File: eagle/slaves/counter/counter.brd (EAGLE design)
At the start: 126.2 x 32 mm, 92 parts, among them IC1 MCP1703DB, IC2 4067D, IC3 74HC154DW, J1 RJ12RIGHTANGLE-I2C, X2 8MHz, X4 MINI-USB

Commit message: change resistor for led
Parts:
- RK11, RK13, RK17, RK19, RK21, RK23, RK25, RK27, RK29, RK31, RK33, RK35, RK41, RK43, RK5, RK9: value 1k -> 100
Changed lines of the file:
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@@
 <?xml version="1.0" encoding="utf-8"?>
 <!DOCTYPE eagle SYSTEM "eagle.dtd">
-<eagle version="8.3.0">
+<eagle version="9.0.0">
 <drawing>
 <settings>
-<setting alwaysvectorfont="yes"/>
+<setting alwaysvectorfont="no"/>
 <setting keepoldvectorfont="yes"/>
 <setting verticaltext="up"/>
@@
 <param name="dpMaxLengthDifference" value="10mm"/>
 <param name="dpGapFactor" value="2.5"/>
-<param name="checkGrid" value="0"/>
 <param name="checkAngle" value="0"/>
 <param name="checkFont" value="1"/>
 <param name="checkRestrict" value="0"/>
+<param name="checkStop" value="0"/>
+<param name="checkValues" value="0"/>
 <param name="useDiameter" value="13"/>
 <param name="maxErrors" value="50"/>
@@
 <element name="IC3" library="74xx-eu" library_urn="urn:adsk.eagle:library:85" package="SO24W" value="74HC154DW" x="50.92" y="24.3625" rot="R270"/>
 <element name="O3" library="SparkFun" package="QRE1113" value="QRE1113" x="3.81" y="12.7" smashed="yes" rot="MR180"/>
-<element name="RK5" library="resistor" package="M0805" value="1k" x="2.54" y="12.7" smashed="yes" rot="R90">
+<element name="RK5" library="resistor" package="M0805" value="100" x="2.54" y="12.7" smashed="yes" rot="R90">
 <attribute name="NAME" x="1.27" y="11.43" size="1.27" layer="25" rot="R90"/>
 <attribute name="VALUE" x="1.42875" y="11.7475" size="1.27" layer="27" rot="R90"/>
@@
 </element>
 <element name="O4" library="SparkFun" package="QRE1113" value="QRE1113" x="3.81" y="3.81" smashed="yes" rot="MR0"/>
-<element name="RK9" library="resistor" package="M0805" value="1k" x="5.08" y="3.81" smashed="yes" rot="R270">
+<element name="RK9" library="resistor" package="M0805" value="100" x="5.08" y="3.81" smashed="yes" rot="R270">
 <attribute name="NAME" x="6.35" y="5.08" size="1.27" layer="25" rot="R270"/>
 <attribute name="VALUE" x="6.0325" y="4.1275" size="1.27" layer="27" rot="R270"/>
@@
 </element>
 <element name="O5" library="SparkFun" package="QRE1113" value="QRE1113" x="16.51" y="12.7" smashed="yes" rot="MR180"/>
-<element name="RK11" library="resistor" package="M0805" value="1k" x="15.24" y="12.7" smashed="yes" rot="R90">
+<element name="RK11" library="resistor" package="M0805" value="100" x="15.24" y="12.7" smashed="yes" rot="R90">
 <attribute name="NAME" x="13.97" y="11.43" size="1.27" layer="25" rot="R90"/>
 <attribute name="VALUE" x="14.12875" y="11.7475" size="1.27" layer="27" rot="R90"/>
@@
 </element>
 <element name="O6" library="SparkFun" package="QRE1113" value="QRE1113" x="16.51" y="3.81" smashed="yes" rot="MR0"/>
-<element name="RK13" library="resistor" package="M0805" value="1k" x="17.78" y="3.81" smashed="yes" rot="R270">
+<element name="RK13" library="resistor" package="M0805" value="100" x="17.78" y="3.81" smashed="yes" rot="R270">
 <attribute name="NAME" x="19.05" y="5.08" size="1.27" layer="25" rot="R270"/>
 <attribute name="VALUE" x="18.7325" y="4.1275" size="1.27" layer="27" rot="R270"/>
@@
 </element>
 <element name="O9" library="SparkFun" package="QRE1113" value="QRE1113" x="29.21" y="12.7" smashed="yes" rot="MR180"/>
-<element name="RK21" library="resistor" package="M0805" value="1k" x="27.94" y="12.7" smashed="yes" rot="R90">
+<element name="RK21" library="resistor" package="M0805" value="100" x="27.94" y="12.7" smashed="yes" rot="R90">
 <attribute name="NAME" x="26.67" y="11.43" size="1.27" layer="25" rot="R90"/>
 <attribute name="VALUE" x="26.82875" y="11.7475" size="1.27" layer="27" rot="R90"/>
@@
 </element>
 <element name="O10" library="SparkFun" package="QRE1113" value="QRE1113" x="29.21" y="3.81" smashed="yes" rot="MR0"/>
-<element name="RK23" library="resistor" package="M0805" value="1k" x="30.48" y="3.81" smashed="yes" rot="R270">
+<element name="RK23" library="resistor" package="M0805" value="100" x="30.48" y="3.81" smashed="yes" rot="R270">
 <attribute name="NAME" x="31.75" y="5.08" size="1.27" layer="25" rot="R270"/>
 <attribute name="VALUE" x="31.4325" y="4.1275" size="1.27" layer="27" rot="R270"/>
@@
 </element>
 <element name="O13" library="SparkFun" package="QRE1113" value="QRE1113" x="42.545" y="12.7" smashed="yes" rot="MR180"/>
-<element name="RK29" library="resistor" package="M0805" value="1k" x="41.275" y="12.7" smashed="yes" rot="R90">
+<element name="RK29" library="resistor" package="M0805" value="100" x="41.275" y="12.7" smashed="yes" rot="R90">
 <attribute name="NAME" x="40.005" y="11.43" size="1.27" layer="25" rot="R90"/>
 <attribute name="VALUE" x="40.16375" y="11.7475" size="1.27" layer="27" rot="R90"/>
@@
 </element>
 <element name="O14" library="SparkFun" package="QRE1113" value="QRE1113" x="42.545" y="3.81" smashed="yes" rot="MR0"/>
-<element name="RK31" library="resistor" package="M0805" value="1k" x="43.815" y="3.81" smashed="yes" rot="R270">
+<element name="RK31" library="resistor" package="M0805" value="100" x="43.815" y="3.81" smashed="yes" rot="R270">
 <attribute name="NAME" x="45.085" y="5.08" size="1.27" layer="25" rot="R270"/>
 <attribute name="VALUE" x="44.7675" y="4.1275" size="1.27" layer="27" rot="R270"/>
@@
 </element>
 <element name="O7" library="SparkFun" package="QRE1113" value="QRE1113" x="55.88" y="12.7" smashed="yes" rot="MR180"/>
-<element name="RK17" library="resistor" package="M0805" value="1k" x="54.61" y="12.7" smashed="yes" rot="R90">
+<element name="RK17" library="resistor" package="M0805" value="100" x="54.61" y="12.7" smashed="yes" rot="R90">
 <attribute name="NAME" x="53.34" y="11.43" size="1.27" layer="25" rot="R90"/>
 <attribute name="VALUE" x="53.49875" y="11.7475" size="1.27" layer="27" rot="R90"/>
@@
 </element>
 <element name="O8" library="SparkFun" package="QRE1113" value="QRE1113" x="55.88" y="3.81" smashed="yes" rot="MR0"/>
-<element name="RK19" library="resistor" package="M0805" value="1k" x="57.15" y="3.81" smashed="yes" rot="R270">
+<element name="RK19" library="resistor" package="M0805" value="100" x="57.15" y="3.81" smashed="yes" rot="R270">
 <attribute name="NAME" x="58.42" y="5.08" size="1.27" layer="25" rot="R270"/>
 <attribute name="VALUE" x="58.1025" y="4.1275" size="1.27" layer="27" rot="R270"/>
@@
 </element>
 <element name="O15" library="SparkFun" package="QRE1113" value="QRE1113" x="69.215" y="12.7" smashed="yes" rot="MR180"/>
-<element name="RK33" library="resistor" package="M0805" value="1k" x="67.945" y="12.7" smashed="yes" rot="R90">
+<element name="RK33" library="resistor" package="M0805" value="100" x="67.945" y="12.7" smashed="yes" rot="R90">
 <attribute name="NAME" x="66.675" y="11.43" size="1.27" layer="25" rot="R90"/>
 <attribute name="VALUE" x="66.83375" y="11.7475" size="1.27" layer="27" rot="R90"/>
@@
 </element>
 <element name="O16" library="SparkFun" package="QRE1113" value="QRE1113" x="69.215" y="3.81" smashed="yes" rot="MR0"/>
-<element name="RK35" library="resistor" package="M0805" value="1k" x="70.485" y="3.81" smashed="yes" rot="R270">
+<element name="RK35" library="resistor" package="M0805" value="100" x="70.485" y="3.81" smashed="yes" rot="R270">
 <attribute name="NAME" x="71.755" y="5.08" size="1.27" layer="25" rot="R270"/>
 <attribute name="VALUE" x="71.4375" y="4.1275" size="1.27" layer="27" rot="R270"/>
@@
 </element>
 <element name="O19" library="SparkFun" package="QRE1113" value="QRE1113" x="82.55" y="12.7" smashed="yes" rot="MR180"/>
-<element name="RK41" library="resistor" package="M0805" value="1k" x="81.28" y="12.7" smashed="yes" rot="R90">
+<element name="RK41" library="resistor" package="M0805" value="100" x="81.28" y="12.7" smashed="yes" rot="R90">
 <attribute name="NAME" x="80.01" y="11.43" size="1.27" layer="25" rot="R90"/>
 <attribute name="VALUE" x="80.16875" y="11.7475" size="1.27" layer="27" rot="R90"/>
@@
 </element>
 <element name="O20" library="SparkFun" package="QRE1113" value="QRE1113" x="82.55" y="3.81" smashed="yes" rot="MR0"/>
-<element name="RK43" library="resistor" package="M0805" value="1k" x="83.82" y="3.81" smashed="yes" rot="R270">
+<element name="RK43" library="resistor" package="M0805" value="100" x="83.82" y="3.81" smashed="yes" rot="R270">
 <attribute name="NAME" x="85.09" y="5.08" size="1.27" layer="25" rot="R270"/>
 <attribute name="VALUE" x="84.7725" y="4.1275" size="1.27" layer="27" rot="R270"/>
@@
 </element>
 <element name="O11" library="SparkFun" package="QRE1113" value="QRE1113" x="95.25" y="12.7" smashed="yes" rot="MR180"/>
-<element name="RK25" library="resistor" package="M0805" value="1k" x="93.98" y="12.7" smashed="yes" rot="R90">
+<element name="RK25" library="resistor" package="M0805" value="100" x="93.98" y="12.7" smashed="yes" rot="R90">
 <attribute name="NAME" x="92.71" y="11.43" size="1.27" layer="25" rot="R90"/>
 <attribute name="VALUE" x="92.86875" y="11.7475" size="1.27" layer="27" rot="R90"/>
@@
 </element>
 <element name="O12" library="SparkFun" package="QRE1113" value="QRE1113" x="95.25" y="3.81" smashed="yes" rot="MR0"/>
-<element name="RK27" library="resistor" package="M0805" value="1k" x="96.52" y="3.81" smashed="yes" rot="R270">
+<element name="RK27" library="resistor" package="M0805" value="100" x="96.52" y="3.81" smashed="yes" rot="R270">
 <attribute name="NAME" x="97.79" y="5.08" size="1.27" layer="25" rot="R270"/>
 <attribute name="VALUE" x="97.4725" y="4.1275" size="1.27" layer="27" rot="R270"/>
@@
 </signal>
 </signals>
-<errors>
-</errors>
 </board>
 </drawing>

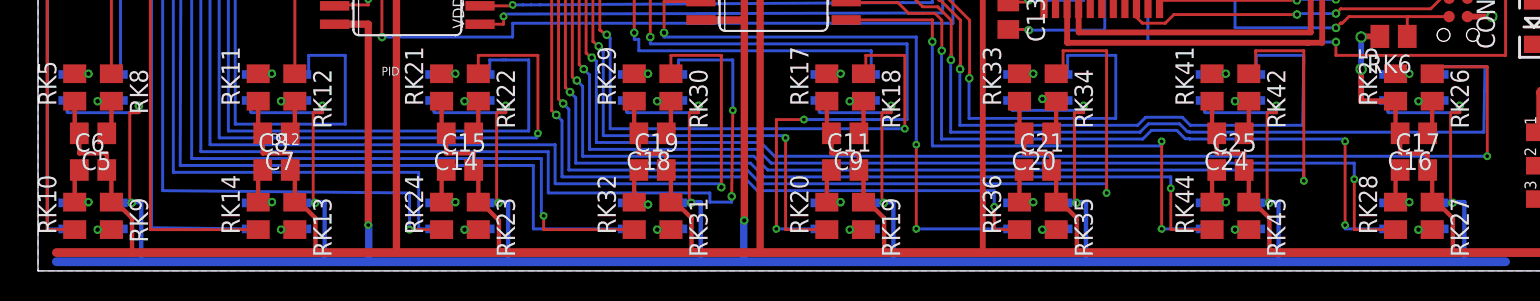
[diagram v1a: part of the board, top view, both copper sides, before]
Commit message: remove 10nf capacitor
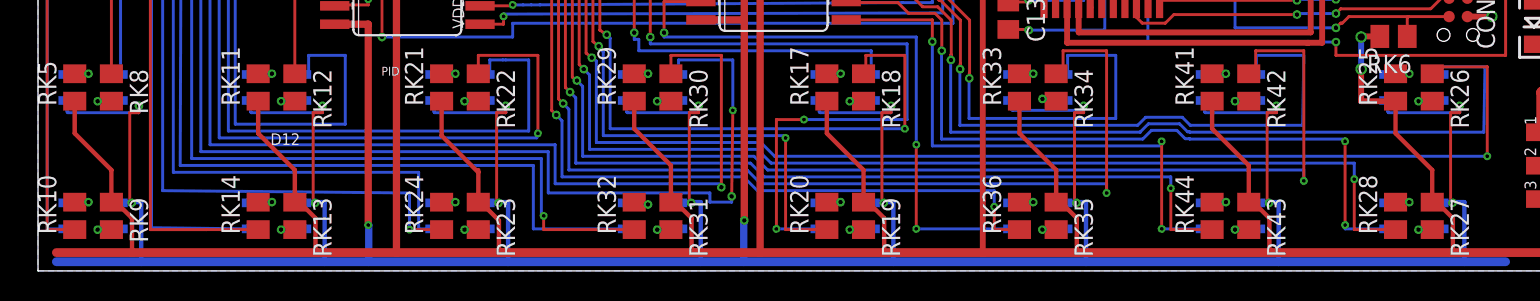
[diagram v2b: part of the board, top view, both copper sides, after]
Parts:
- removed C11, C14, C15, C16, C17, C18, C19, C20, C21, C24, C25, C5, C6, C7, C8, C9: 10n, rcl:C0805
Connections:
- net 3.3V: no longer C11.2, C14.2, C15.2, C16.2, C17.2, C18.2, C19.2, C20.2, C21.2, C24.2, C25.2, C5.2, C6.2, C7.2, C8.2, C9.2
- net Y10: no longer C15.1
- net Y11: no longer C16.1
- net Y12: no longer C17.1
- net Y13: no longer C18.1
- net Y14: no longer C19.1
- net Y15: no longer C20.1
- net Y16: no longer C21.1
- net Y19: no longer C24.1
- net Y20: no longer C25.1
- net Y3: no longer C5.1
- net Y4: no longer C6.1
- net Y5: no longer C7.1
- net Y6: no longer C8.1
- net Y7: no longer C9.1
- net Y8: no longer C11.1
- net Y9: no longer C14.1
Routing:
- net 3.3V: track 379.2 -> 369.0 mm
- net Y16: track 5.03 -> 2.49 mm
- net Y8: track 5.04 -> 2.49 mm
- net Y6: track 5.03 -> 2.49 mm
- net Y14: track 5.10 -> 2.56 mm
- net Y10: track 5.03 -> 2.49 mm
- net Y4: track 5.04 -> 2.49 mm
- net Y20: track 5.03 -> 2.49 mm
- net Y12: track 5.03 -> 2.49 mm
- net Y3: track 4.85 -> 2.49 mm
- net Y9: track 4.85 -> 2.49 mm
- net Y7: track 4.85 -> 2.49 mm
- net Y5: track 4.85 -> 2.49 mm
- net Y13: track 4.85 -> 2.49 mm
- net Y19: track 4.85 -> 2.49 mm
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
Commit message: change resistor to 1k
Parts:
- RK10, RK12, RK14, RK18, RK20, RK22, RK24, RK26, RK28, RK30, RK32, RK34, RK36, RK42, RK44, RK8: value 220 -> 1k
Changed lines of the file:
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@@
 <grid distance="6.25" unitdist="mil" unit="mil" style="lines" multiple="10" display="yes" altdistance="3.125" altunitdist="mil" altunit="mil"/>
 <layers>
-<layer number="1" name="Top" color="4" fill="1" visible="yes" active="yes"/>
+<layer number="1" name="Top" color="4" fill="1" visible="no" active="yes"/>
 <layer number="16" name="Bottom" color="1" fill="1" visible="yes" active="yes"/>
 <layer number="17" name="Pads" color="2" fill="1" visible="yes" active="yes"/>
@@
 <attribute name="VALUE" x="1.42875" y="11.7475" size="1.27" layer="27" rot="R90"/>
 </element>
-<element name="RK8" library="resistor" package="M0805" value="220" x="5.08" y="12.7" smashed="yes" rot="R270">
+<element name="RK8" library="resistor" package="M0805" value="1k" x="5.08" y="12.7" smashed="yes" rot="R270">
 <attribute name="NAME" x="6.35" y="13.97" size="1.27" layer="25" rot="R270"/>
 <attribute name="VALUE" x="6.19125" y="14.605" size="1.27" layer="27" rot="R270"/>
@@
 <attribute name="VALUE" x="6.0325" y="4.1275" size="1.27" layer="27" rot="R270"/>
 </element>
-<element name="RK10" library="resistor" package="M0805" value="220" x="2.54" y="3.81" smashed="yes" rot="R90">
+<element name="RK10" library="resistor" package="M0805" value="1k" x="2.54" y="3.81" smashed="yes" rot="R90">
 <attribute name="NAME" x="1.27" y="2.54" size="1.27" layer="25" rot="R90"/>
 <attribute name="VALUE" x="1.42875" y="2.54" size="1.27" layer="27" rot="R90"/>
@@
 <attribute name="VALUE" x="14.12875" y="11.7475" size="1.27" layer="27" rot="R90"/>
 </element>
-<element name="RK12" library="resistor" package="M0805" value="220" x="17.78" y="12.7" smashed="yes" rot="R270">
+<element name="RK12" library="resistor" package="M0805" value="1k" x="17.78" y="12.7" smashed="yes" rot="R270">
 <attribute name="NAME" x="19.05" y="13.97" size="1.27" layer="25" rot="R270"/>
 <attribute name="VALUE" x="18.89125" y="14.605" size="1.27" layer="27" rot="R270"/>
@@
 <attribute name="VALUE" x="18.7325" y="4.1275" size="1.27" layer="27" rot="R270"/>
 </element>
-<element name="RK14" library="resistor" package="M0805" value="220" x="15.24" y="3.81" smashed="yes" rot="R90">
+<element name="RK14" library="resistor" package="M0805" value="1k" x="15.24" y="3.81" smashed="yes" rot="R90">
 <attribute name="NAME" x="13.97" y="2.54" size="1.27" layer="25" rot="R90"/>
 <attribute name="VALUE" x="14.12875" y="2.54" size="1.27" layer="27" rot="R90"/>
@@
 <attribute name="VALUE" x="26.82875" y="11.7475" size="1.27" layer="27" rot="R90"/>
 </element>
-<element name="RK22" library="resistor" package="M0805" value="220" x="30.48" y="12.7" smashed="yes" rot="R270">
+<element name="RK22" library="resistor" package="M0805" value="1k" x="30.48" y="12.7" smashed="yes" rot="R270">
 <attribute name="NAME" x="31.75" y="13.97" size="1.27" layer="25" rot="R270"/>
 <attribute name="VALUE" x="31.59125" y="14.605" size="1.27" layer="27" rot="R270"/>
@@
 <attribute name="VALUE" x="31.4325" y="4.1275" size="1.27" layer="27" rot="R270"/>
 </element>
-<element name="RK24" library="resistor" package="M0805" value="220" x="27.94" y="3.81" smashed="yes" rot="R90">
+<element name="RK24" library="resistor" package="M0805" value="1k" x="27.94" y="3.81" smashed="yes" rot="R90">
 <attribute name="NAME" x="26.67" y="2.54" size="1.27" layer="25" rot="R90"/>
 <attribute name="VALUE" x="26.82875" y="2.54" size="1.27" layer="27" rot="R90"/>
@@
 <attribute name="VALUE" x="40.16375" y="11.7475" size="1.27" layer="27" rot="R90"/>
 </element>
-<element name="RK30" library="resistor" package="M0805" value="220" x="43.815" y="12.7" smashed="yes" rot="R270">
+<element name="RK30" library="resistor" package="M0805" value="1k" x="43.815" y="12.7" smashed="yes" rot="R270">
 <attribute name="NAME" x="45.085" y="13.97" size="1.27" layer="25" rot="R270"/>
 <attribute name="VALUE" x="44.92625" y="14.605" size="1.27" layer="27" rot="R270"/>
@@
 <attribute name="VALUE" x="44.7675" y="4.1275" size="1.27" layer="27" rot="R270"/>
 </element>
-<element name="RK32" library="resistor" package="M0805" value="220" x="41.275" y="3.81" smashed="yes" rot="R90">
+<element name="RK32" library="resistor" package="M0805" value="1k" x="41.275" y="3.81" smashed="yes" rot="R90">
 <attribute name="NAME" x="40.005" y="2.54" size="1.27" layer="25" rot="R90"/>
 <attribute name="VALUE" x="40.16375" y="2.54" size="1.27" layer="27" rot="R90"/>
@@
 <attribute name="VALUE" x="53.49875" y="11.7475" size="1.27" layer="27" rot="R90"/>
 </element>
-<element name="RK18" library="resistor" package="M0805" value="220" x="57.15" y="12.7" smashed="yes" rot="R270">
+<element name="RK18" library="resistor" package="M0805" value="1k" x="57.15" y="12.7" smashed="yes" rot="R270">
 <attribute name="NAME" x="58.42" y="13.97" size="1.27" layer="25" rot="R270"/>
 <attribute name="VALUE" x="58.26125" y="14.605" size="1.27" layer="27" rot="R270"/>
@@
 <attribute name="VALUE" x="58.1025" y="4.1275" size="1.27" layer="27" rot="R270"/>
 </element>
-<element name="RK20" library="resistor" package="M0805" value="220" x="54.61" y="3.81" smashed="yes" rot="R90">
+<element name="RK20" library="resistor" package="M0805" value="1k" x="54.61" y="3.81" smashed="yes" rot="R90">
 <attribute name="NAME" x="53.34" y="2.54" size="1.27" layer="25" rot="R90"/>
 <attribute name="VALUE" x="53.49875" y="2.54" size="1.27" layer="27" rot="R90"/>
@@
 <attribute name="VALUE" x="66.83375" y="11.7475" size="1.27" layer="27" rot="R90"/>
 </element>
-<element name="RK34" library="resistor" package="M0805" value="220" x="70.485" y="12.7" smashed="yes" rot="R270">
+<element name="RK34" library="resistor" package="M0805" value="1k" x="70.485" y="12.7" smashed="yes" rot="R270">
 <attribute name="NAME" x="71.755" y="13.97" size="1.27" layer="25" rot="R270"/>
 <attribute name="VALUE" x="71.59625" y="14.605" size="1.27" layer="27" rot="R270"/>
@@
 <attribute name="VALUE" x="71.4375" y="4.1275" size="1.27" layer="27" rot="R270"/>
 </element>
-<element name="RK36" library="resistor" package="M0805" value="220" x="67.945" y="3.81" smashed="yes" rot="R90">
+<element name="RK36" library="resistor" package="M0805" value="1k" x="67.945" y="3.81" smashed="yes" rot="R90">
 <attribute name="NAME" x="66.675" y="2.54" size="1.27" layer="25" rot="R90"/>
 <attribute name="VALUE" x="66.83375" y="2.54" size="1.27" layer="27" rot="R90"/>
@@
 <attribute name="VALUE" x="80.16875" y="11.7475" size="1.27" layer="27" rot="R90"/>
 </element>
-<element name="RK42" library="resistor" package="M0805" value="220" x="83.82" y="12.7" smashed="yes" rot="R270">
+<element name="RK42" library="resistor" package="M0805" value="1k" x="83.82" y="12.7" smashed="yes" rot="R270">
 <attribute name="NAME" x="85.09" y="13.97" size="1.27" layer="25" rot="R270"/>
 <attribute name="VALUE" x="84.93125" y="14.605" size="1.27" layer="27" rot="R270"/>
@@
 <attribute name="VALUE" x="84.7725" y="4.1275" size="1.27" layer="27" rot="R270"/>
 </element>
-<element name="RK44" library="resistor" package="M0805" value="220" x="81.28" y="3.81" smashed="yes" rot="R90">
+<element name="RK44" library="resistor" package="M0805" value="1k" x="81.28" y="3.81" smashed="yes" rot="R90">
 <attribute name="NAME" x="80.01" y="2.54" size="1.27" layer="25" rot="R90"/>
 <attribute name="VALUE" x="80.16875" y="2.54" size="1.27" layer="27" rot="R90"/>
@@
 <attribute name="VALUE" x="92.86875" y="11.7475" size="1.27" layer="27" rot="R90"/>
 </element>
-<element name="RK26" library="resistor" package="M0805" value="220" x="96.52" y="12.7" smashed="yes" rot="R270">
+<element name="RK26" library="resistor" package="M0805" value="1k" x="96.52" y="12.7" smashed="yes" rot="R270">
 <attribute name="NAME" x="97.79" y="13.97" size="1.27" layer="25" rot="R270"/>
 <attribute name="VALUE" x="97.63125" y="14.605" size="1.27" layer="27" rot="R270"/>
@@
 <attribute name="VALUE" x="97.4725" y="4.1275" size="1.27" layer="27" rot="R270"/>
 </element>
-<element name="RK28" library="resistor" package="M0805" value="220" x="93.98" y="3.81" smashed="yes" rot="R90">
+<element name="RK28" library="resistor" package="M0805" value="1k" x="93.98" y="3.81" smashed="yes" rot="R90">
 <attribute name="NAME" x="92.71" y="2.54" size="1.27" layer="25" rot="R90"/>
 <attribute name="VALUE" x="92.86875" y="2.54" size="1.27" layer="27" rot="R90"/>
